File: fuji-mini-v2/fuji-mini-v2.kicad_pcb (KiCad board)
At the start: 2 copper layers, 58.4 x 81.3 mm, 59 parts, among them J1 Micro_SD_Card, J2 AudioJack3_SwitchT, J4 USB_C_Receptacle_USB2.0_14P, SW1 RotaryEncoder_Switch, U1 ESP32-S3, U2 PCM5102A, U3 TPA6110A2DGN, U4 ER_OLEDM0.91_1x-I2C, U5 MCP73831-2-MC, U6 AMS1117-3.3

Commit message: v2.0 2.0 Whole Remake
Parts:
- removed BCKWRD/FRWD1, PLAY/PAUSE1: SW_Push, Button_Switch_THT:SW_PUSH_6mm
- removed C23: 10uF, Capacitor_SMD:C_0805_2012Metric
- removed J4: USB_C_Receptacle_USB2.0_14P, Connector_USB:USB_C_Receptacle_XKB_U262-16XN-4BVC11
- removed SW1: RotaryEncoder_Switch, Rotary_Encoder:RotaryEncoder_Alps_EC11E-Switch_Vertical_H20mm
- added BOOT: SW_Push, Button_Switch_THT:SW_PUSH_6mm, F.Cu at (91.4, 134.9)
- added J3: USB_C, Connector_USB:USB_C_Receptacle_XKB_U262-16XN-4BVC11, F.Cu at (81.3, 146.1)
- added NEXT: SW_Push, Button_Switch_THT:SW_PUSH_6mm, F.Cu at (79.9, 106.0)
- added PLAY: SW_Push, Button_Switch_THT:SW_PUSH_6mm, F.Cu at (79.9, 94.6)
- added R22: 5.1k, Resistor_SMD:R_0805_2012Metric, F.Cu at (84.5, 137.8)
- added R23: 5.1k, Resistor_SMD:R_0805_2012Metric, F.Cu at (78.4, 137.8)
- added RESET: SW_Push, Button_Switch_THT:SW_PUSH_6mm, F.Cu at (91.4, 124.1)
- added VOLUME: RotaryEncoder_Switch, Rotary_Encoder:RotaryEncoder_Alps_EC11E-Switch_Vertical_H20mm, F.Cu at (144.1, 56.9)
- BT1: moved to B.Cu
- C1, C5: value 100nF -> 10uF
- C11, C16: value 100nF -> 2.2uF
- C14, C7, J1, R1, R12, R15, R17, R2, R3, R4, R8, R9: moved to F.Cu
- C15: value 1uF -> 100nF
- C17: value 100nF -> 220uF; footprint Capacitor_SMD:C_0805_2012Metric -> Capacitor_THT:CP_Radial_D6.3mm_P2.50mm
- C19: value 220uF -> 4.7uF; footprint Capacitor_THT:CP_Radial_D6.3mm_P2.50mm -> Capacitor_SMD:C_0805_2012Metric
- C20: value 1uF -> 10uF
- C21, C22: value 10uF -> 1uF
- C3: value 100nF -> 1uF
- R10: value 4.7k -> 20k; moved to F.Cu
- R11: value 4.7k -> 10k; moved to F.Cu
- R13, R14: value 10k -> 4.7k; moved to F.Cu
- R16: value 2k -> 10k; moved to F.Cu
- R18: value 5.1k -> 2k; moved to F.Cu
- R19: value 5.1k -> 10k; moved to F.Cu
- R20: value 10k -> 1k; moved to F.Cu
- R21: value 1k -> 10k; moved to F.Cu
- R5, R6, R7: value 20k -> 10k; moved to F.Cu
- U1: value ESP32-S3 -> ESP32-S3-WROOM-1; footprint Package_DFN_QFN:QFN-56-1EP_7x7mm_P0.4mm_EP4x4mm -> RF_Module:ESP32-S3-WROOM-1
- U6: value AMS1117-3.3 -> AP2112K-3.3; footprint Package_TO_SOT_SMD:SOT-223-3_TabPin2 -> Package_TO_SOT_SMD:SOT-23-5
- moved R13 74.7 mm to (99.3, 61.0), turned to 0 degrees
- moved BT1 72.5 mm to (78.2, 69.5), turned to -90 degrees
- moved R15 71.3 mm to (140.3, 80.0), turned to 0 degrees
- moved R19 57.0 mm to (145.8, 80.0), turned to 0 degrees
- moved J2 54.1 mm to (142.2, 135.3), turned to 0 degrees
- moved R18 53.5 mm to (78.5, 78.7), turned to 0 degrees
- moved D1 53.3 mm to (79.4, 61.6)
- moved R14 51.4 mm to (94.3, 61.0), turned to 0 degrees
- moved U5 50.4 mm to (80.9, 87.5)
- moved C2 49.2 mm to (140.3, 92.1)
- moved C4 48.6 mm to (87.0, 119.4)
- moved C17 47.3 mm to (132.1, 137.2)
- moved R10 46.1 mm to (137.2, 125.5), turned to 90 degrees
- moved C8 45.3 mm to (143.2, 123.2)
- moved C19 43.6 mm to (90.8, 87.3), turned to 90 degrees
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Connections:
- BT1 pad 2: 3V3 -> GND
- C1 pad 1: 3V3 -> +3V3
- C1 pad 2: Net-(J1-VDD) -> GND
- C10 pad 1: 3V3 -> GND
- C10 pad 2: 3V3 -> +3V3
- C11 pad 1: 3V3 -> Net-(U2-CAPP)
- C11 pad 2: 3V3 -> Net-(U2-CAPM)
- C12 pad 1: Net-(U2-CAPP) -> Net-(U3-BYPASS)
- C12 pad 2: Net-(U2-CAPM) -> GND
- C13 pad 1: Net-(U3-BYPASS) -> Net-(U2-OUTL)
- C13 pad 2: 3V3 -> DAC_OUTL
- C14 pad 1: Net-(U2-OUTL) -> Net-(U2-OUTR)
- C14 pad 2: DAC_OUTL -> DAC_OUTR
- C15 pad 1: Net-(U2-OUTR) -> Net-(U2-LDOO)
- C15 pad 2: DAC_OUTR -> GND
- C16 pad 1: Net-(U2-LDOO) -> Net-(U2-VNEG)
- C16 pad 2: 3V3 -> GND
- C17 pad 1: Net-(U2-VNEG) -> VO1
- C17 pad 2: 3V3 -> HP_L
- C18 pad 1: VO1 -> VO2
- C18 pad 2: HP_L -> HP_R
- C19 pad 1: VO2 -> GND
- C19 pad 2: HP_R -> VDD
- C2 pad 1: 3V3 -> +3V3
- C2 pad 2: 3V3 -> GND
- C20 pad 1: 3V3 -> GND
- C20 pad 2: VDD -> VBAT
- C21 pad 1: 3V3 -> GND
- C22 pad 1: 3V3 -> +3V3
- C22 pad 2: 3V3 -> GND
- C3 pad 1: 3V3 -> GND
- C3 pad 2: 3V3 -> Net-(U1-EN)
- C4 pad 1: 3V3 -> +3V3
- C4 pad 2: 3V3 -> GND
- C5 pad 1: 3V3 -> +3V3
- C5 pad 2: 3V3 -> GND
- C6 pad 1: 3V3 -> +3V3
- C6 pad 2: 3V3 -> GND
- C7 pad 1: 3V3 -> +3V3
- C7 pad 2: 3V3 -> GND
- C8 pad 1: 3V3 -> +3V3
- C8 pad 2: 3V3 -> GND
- C9 pad 1: 3V3 -> +3V3
- C9 pad 2: 3V3 -> GND
- D1 pad 2: 3V3 -> +3V3
- J1 pad 4: Net-(J1-VDD) -> +3V3
- J1 pad 6: 3V3 -> GND
- J1 pad SH: 3V3 -> GND
- J2 pad S: 3V3 -> GND
- J2 pad TN: HP_DETECT -> unconnected-(J2-PadTN)
- R1 pad 1: 3V3 -> GPIO11
- R1 pad 2: Net-(J1-DAT2) -> +3V3
- R10 pad 1: I2C_SCL -> DAC_OUTL
- R10 pad 2: 3V3 -> Net-(U3-IN1-)
- R11 pad 1: 3V3 -> VO1
- R11 pad 2: I2C_SDA -> Net-(U3-IN1-)
- R12 pad 1: 3V3 -> GND
- R12 pad 2: ENC_A -> AMP_ENABLE
- R13 pad 1: 3V3 -> I2C_SCL
- R13 pad 2: ENC_B -> +3V3
- R14 pad 1: BTN_PLAY -> +3V3
- R14 pad 2: 3V3 -> I2C_SDA
- R15 pad 1: 3V3 -> +3V3
- R15 pad 2: HP_DETECT -> ENC_A
- R16 pad 1: 3V3 -> +3V3
- R16 pad 2: Net-(U5-PROG) -> ENC_B
- R17 pad 1: Net-(R17-Pad1) -> BTN_PLAY
- R17 pad 2: 3V3 -> +3V3
- R18 pad 1: 3V3 -> GND
- R18 pad 2: Net-(J4-CC1) -> Net-(U5-PROG)
- R19 pad 1: 3V3 -> ENC_BTN
- R19 pad 2: Net-(J4-CC2) -> +3V3
- R2 pad 1: 3V3 -> +3V3
- R2 pad 2: Net-(J1-DAT1) -> GPIO10
- R20 pad 1: 3V3 -> Net-(U5-STAT)
- R20 pad 2: BTN_NEXT -> Net-(D1-K)
- R21 pad 1: Net-(U5-STAT) -> +3V3
- R21 pad 2: Net-(D1-K) -> BTN_NEXT
- R3 pad 1: Net-(U1-CHIP_PU) -> GPIO13
- R3 pad 2: 3V3 -> +3V3
- R4 pad 1: DAC_MUTE -> +3V3
- R4 pad 2: 3V3 -> Net-(U1-EN)
- R5 pad 1: DAC_OUTR -> +3V3
- R5 pad 2: Net-(U3-IN2-) -> Net-(J1-DAT1)
- R6 pad 1: VO2 -> +3V3
- R6 pad 2: Net-(U3-IN2-) -> Net-(J1-DAT2)
- R7 pad 1: DAC_OUTL -> DAC_MUTE
- R7 pad 2: Net-(U3-IN1-) -> GND
- R8 pad 1: VO1 -> DAC_OUTR
- R8 pad 2: Net-(U3-IN1-) -> Net-(U3-IN2-)
- R9 pad 1: 3V3 -> VO2
- R9 pad 2: AMP_ENABLE -> Net-(U3-IN2-)
- U1 pad 1: unconnected-(U1-LNA_IN-Pad1) -> GND
- U1 pad 10: I2S_BCK -> AMP_ENABLE
- U1 pad 11: I2S_DIN -> BTN_PLAY
- U1 pad 12: I2S_SCK -> I2C_SCL
- U1 pad 13: I2C_SCL -> USB_DN
- U1 pad 14: I2C_SDA -> USB_DP
- U1 pad 15: GPIO10 -> unconnected-(U1-IO3-Pad15)
- U1 pad 16: GPIO11 -> unconnected-(U1-IO46-Pad16)
- U1 pad 17: GPIO12 -> I2C_SDA
- U1 pad 18: GPIO13 -> GPIO10
- U1 pad 19: DAC_MUTE -> GPIO11
- U1 pad 2: 3V3 -> +3V3
- U1 pad 20: 3V3 -> GPIO12
- U1 pad 21: unconnected-(U1-XTAL_32K_P-Pad21) -> GPIO13
- U1 pad 22: unconnected-(U1-XTAL_32K_N-Pad22) -> DAC_MUTE
- U1 pad 23: AMP_ENABLE -> unconnected-(U1-IO21-Pad23)
- U1 pad 25: USB_DN -> unconnected-(U1-IO48-Pad25)
- U1 pad 26: USB_DP -> unconnected-(U1-IO45-Pad26)
- U1 pad 27: unconnected-(U1-GPIO21-Pad27) -> Net-(U1-IO0)
- U1 pad 29: 3V3 -> unconnected-(U1-IO36-Pad29)
- U1 pad 3: 3V3 -> Net-(U1-EN)
- U1 pad 38: unconnected-(U1-GPIO33-Pad38) -> ENC_B
- U1 pad 39: unconnected-(U1-GPIO34-Pad39) -> ENC_A
- U1 pad 4: Net-(U1-CHIP_PU) -> I2S_LRCK
- U1 pad 40: unconnected-(U1-GPIO35-Pad40) -> GND
- U1 pad 41: unconnected-(U1-GPIO36-Pad41) -> GND
- U1 pad 5: unconnected-(U1-GPIO0-Pad5) -> I2S_BCK
- U1 pad 6: unconnected-(U1-GPIO1-Pad6) -> I2S_DIN
- U1 pad 7: unconnected-(U1-GPIO2-Pad7) -> I2S_SCK
- U1 pad 8: unconnected-(U1-GPIO3-Pad8) -> ENC_BTN
- U1 pad 9: I2S_LRCK -> BTN_NEXT
- U2 pad 1: 3V3 -> +3V3
- U2 pad 10: 3V3 -> GND
- U2 pad 11: 3V3 -> GND
- U2 pad 16: 3V3 -> GND
- U2 pad 19: 3V3 -> GND
- U2 pad 20: 3V3 -> +3V3
- U2 pad 3: 3V3 -> GND
- U2 pad 8: 3V3 -> +3V3
- U2 pad 9: 3V3 -> GND
- U3 pad 2: 3V3 -> GND
- U3 pad 6: 3V3 -> +3V3
- U3 pad 9: 3V3 -> GND
- U4 pad 1: 3V3 -> GND
- U4 pad 2: 3V3 -> +3V3
- U5 pad 6: 3V3 -> GND
- U6 pad 1: 3V3 -> VBAT
- U6 pad 2: 3V3 -> GND
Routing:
- net 3V3: track 685.5 -> 0.00 mm, vias 16 -> 0
- net GND: track 0.00 -> 596.1 mm, vias 0 -> 14
- net +3V3: track 0.00 -> 353.4 mm, vias 0 -> 17
- net Net-(U2-VNEG): track 151.2 -> 12.8 mm, vias 2 -> 0
- net BTN_NEXT: track 10.6 -> 144.3 mm, vias 0 -> 2
- net ENC_B: track 4.21 -> 113.6 mm, vias 0 -> 2
- net ENC_A: track 4.35 -> 112.6 mm, vias 0 -> 2
- net Net-(D1-K): track 119.7 -> 17.7 mm, vias 0 -> 2
- net Net-(U2-CAPM): track 103.9 -> 9.84 mm, vias 2 -> 0
- net I2C_SCL: track 38.8 -> 129.9 mm, vias 1 -> 2
- net ENC_BTN: track 0.00 -> 88.7 mm, vias 0 -> 2
- net BTN_PLAY: track 11.4 -> 94.8 mm, vias 0 -> 3
- net I2C_SDA: track 49.4 -> 132.7 mm, vias 1 -> 2
- net Net-(U1-IO0): track 0.00 -> 73.0 mm
- net I2S_LRCK: track 115.4 -> 45.9 mm, vias 6 -> 4
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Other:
- board size 58.4 x 81.3 mm -> 73.8 x 97.7 mm
- board text removed: "Made by A41K"

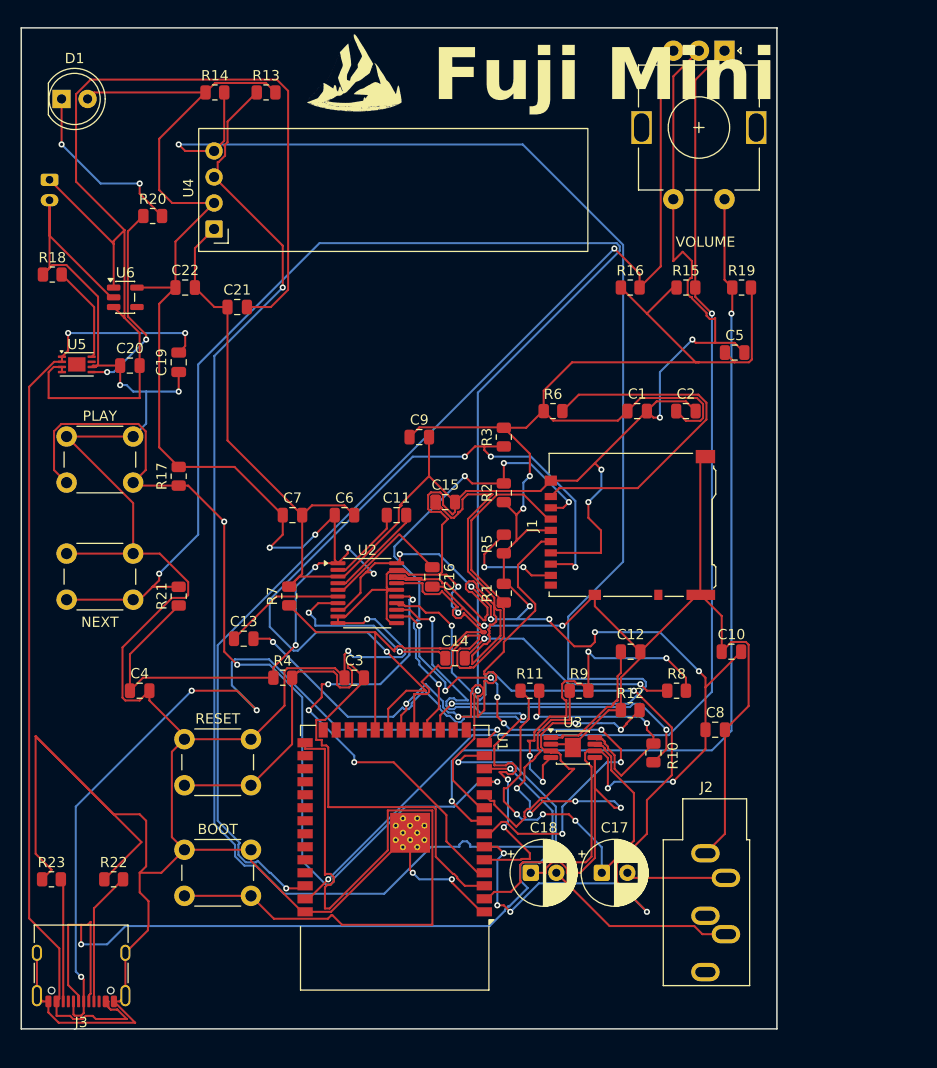
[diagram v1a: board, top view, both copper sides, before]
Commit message: Added 3D models / Fixed PCB positions
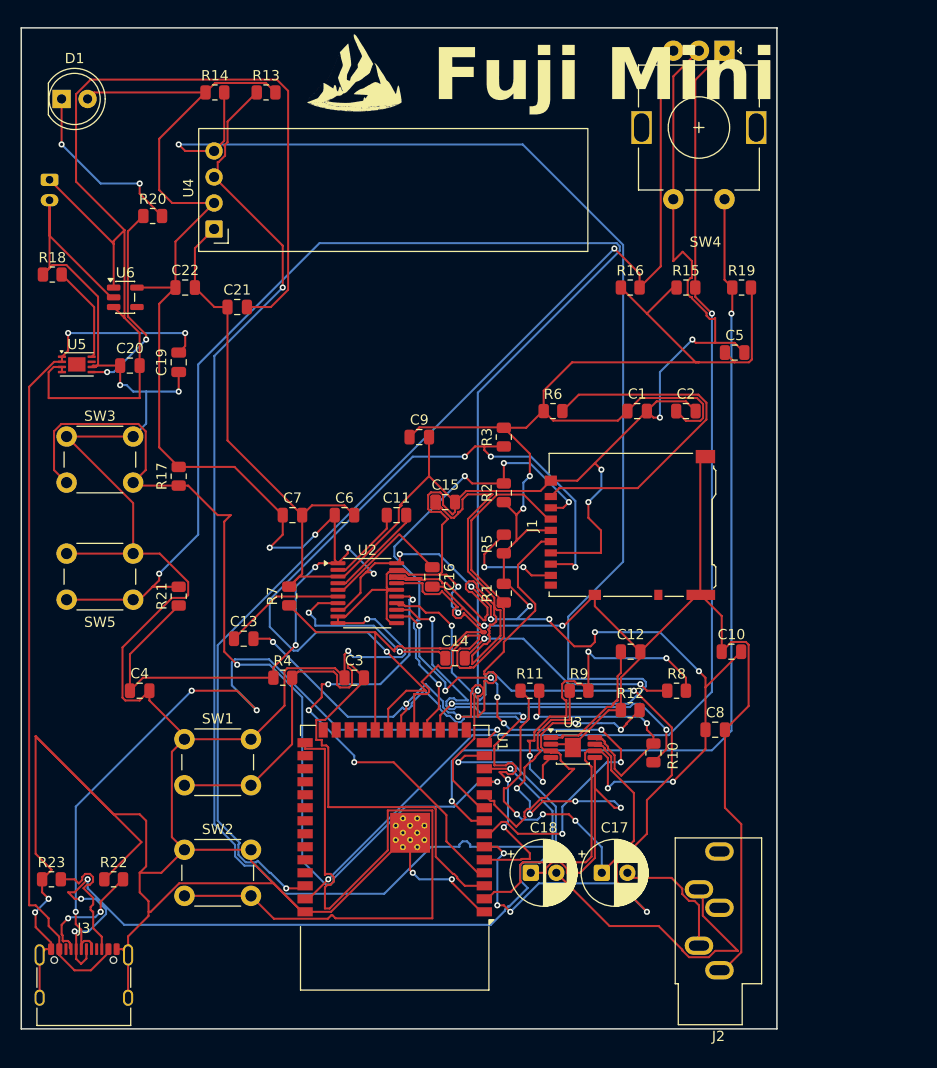
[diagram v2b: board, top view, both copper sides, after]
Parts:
- J3: value USB_C -> USB_C_Receptacle_USB2.0_14P
- moved J2 11.5 mm to (143.6, 146.7), turned to 180 degrees
- moved J3 2.25 mm to (81.5, 148.3), turned to 0 degrees
- renumbered RESET to SW1, BOOT to SW2, PLAY to SW3, VOLUME to SW4, NEXT to SW5
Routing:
- net GND: track 596.1 -> 621.3 mm, vias 14 -> 16
- net HP_R: track 19.0 -> 29.0 mm
- net VDD: track 94.0 -> 84.4 mm
- net USB_DP: track 82.4 -> 76.0 mm
- net USB_DN: track 90.8 -> 87.9 mm, vias 2 -> 4
- net HP_L: track 9.83 -> 12.6 mm
- net Net-(J3-CC1): track 13.1 -> 11.5 mm, vias 0 -> 2
- net BTN_PLAY: track 94.8 -> 96.1 mm, vias 3 -> 2
- net Net-(U1-IO0): track 73.0 -> 72.1 mm
- net Net-(J3-CC2): track 12.0 -> 12.9 mm

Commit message: Finished / Started the README / Added new gerbers
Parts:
- Headphone Jack: renamed from J2
- renumbered J3 to USB-C
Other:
- board text added: "v1.0"
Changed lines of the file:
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@@
 		(tags "tact sw push 6mm")
 		(property "Reference" "SW5"
-			(at 3.25 6.695 0)
+			(at 3.25 -2.485 0)
 			(layer "F.SilkS")
 			(effects
@@
 		(descr "USB Type C, right-angle, SMT, https://datasheet.lcsc.com/szlcsc/1811141824_XKB-Enterprise-U262-161N-4BVC11_C319148.pdf")
 		(tags "USB C Type-C Receptacle SMD")
-		(property "Reference" "J3"
+		(property "Reference" "USB-C"
 			(at 0 -5.715 0)
 			(layer "F.SilkS")
@@
 		(descr "TRS 3.5mm, horizontal, through-hole, with switch, https://www.cui.com/product/resource/sj1-353xng.pdf")
 		(tags "TRS audio jack stereo horizontal")
-		(property "Reference" "J2"
-			(at 0.1 -6.45 0)
+		(property "Reference" "Headphone Jack"
+			(at 5.815 0.625 90)
 			(layer "F.SilkS")
 			(effects
@@
 				)
 			)
+		)
+	)
+	(gr_text "v1.0"
+		(at 147.955 95.885 90)
+		(layer "F.SilkS")
+		(effects
+			(font
+				(face "Gadugi")
+				(size 2 2)
+				(thickness 0.3048)
+				(bold yes)
+			)
+			(justify left bottom)
+		)
+		(render_cache "v1.0" 90
+			(polygon
+				(pts
+					(xy 146.215976 94.371182) (xy 147.615 94.891664) (xy 147.615 95.383569) (xy 146.215976 95.879504)
+					(xy 146.215976 95.417763) (xy 147.078032 95.174619) (xy 147.219638 95.140928) (xy 147.326671 95.126748)
+					(xy 147.326671 95.121252) (xy 147.224676 95.105221) (xy 147.086214 95.070694) (xy 146.215976 94.822055)
+				)
+			)
+			(polygon
+				(pts
+					(xy 145.614162 93.232034) (xy 147.615 93.232034) (xy 147.615 93.66239) (xy 146.100083 93.66239)
+					(xy 146.159434 93.746409) (xy 146.209993 93.849602) (xy 146.248217 93.96293) (xy 146.270687 94.079068)
+					(xy 145.911161 94.079068) (xy 145.854223 93.914988) (xy 145.784155 93.762163) (xy 145.70186 93.618665)
+					(xy 145.614162 93.493007)
+				)
+			)
+			(polygon
+				(pts
+					(xy 147.646263 92.384389) (xy 147.638621 92.452784) (xy 147.616636 92.511232) (xy 147.580317 92.561953)
+					(xy 147.532604 92.601687) (xy 147.47926 92.625055) (xy 147.418262 92.633028) (xy 147.355644 92.624731)
+					(xy 147.302408 92.600658) (xy 147.256207 92.56) (xy 147.221516 92.508127) (xy 147.20034 92.448052)
+					(xy 147.192948 92.37755) (xy 147.200496 92.306171) (xy 147.221938 92.24665) (xy 147.256817 92.196444)
+					(xy 147.303238 92.157306) (xy 147.356317 92.134093) (xy 147.418262 92.126102) (xy 147.481884 92.134306)
+					(xy 147.535803 92.158038) (xy 147.582393 92.197909) (xy 147.617144 92.249023) (xy 147.638652 92.310273)
+				)
+			)
+			(polygon
+				(pts
+					(xy 146.826795 90.49439) (xy 147.002499 90.51954) (xy 147.151111 90.558536) (xy 147.276367 90.609664)
+					(xy 147.381503 90.67188) (xy 147.477102 90.753245) (xy 147.550055 90.845563) (xy 147.602489 90.950208)
+					(xy 147.634932 91.069549) (xy 147.646263 91.206772) (xy 147.634375 91.352265) (xy 147.600724 91.475667)
+					(xy 147.546941 91.581031) (xy 147.47273 91.671359) (xy 147.375905 91.748349) (xy 147.252577 91.812238)
+					(xy 147.097427 91.861787) (xy 146.903973 91.894398) (xy 146.664773 91.906284) (xy 146.452276 91.897109)
+					(xy 146.272635 91.871489) (xy 146.121412 91.83186) (xy 145.994621 91.780033) (xy 145.888813 91.717117)
+					(xy 145.792846 91.634701) (xy 145.719369 91.540616) (xy 145.666379 91.433377) (xy 145.633491 91.31047)
+					(xy 145.623523 91.187599) (xy 145.95024 91.187599) (xy 145.963705 91.259708) (xy 146.004286 91.321303)
+					(xy 146.0783 91.375567) (xy 146.19876 91.421563) (xy 146.383602 91.454719) (xy 146.654637 91.467745)
+					(xy 146.908315 91.455152) (xy 147.081944 91.423035) (xy 147.195693 91.37832) (xy 147.266093 91.325259)
+					(xy 147.305011 91.264582) (xy 147.318 91.193094) (xy 147.305049 91.124457) (xy 147.265924 91.065682)
+					(xy 147.194339 91.013756) (xy 147.077509 90.969643) (xy 146.897877 90.937802) (xy 146.63412 90.925282)
+					(xy 146.369544 90.937632) (xy 146.189681 90.96901) (xy 146.073012 91.012403) (xy 146.001791 91.063333)
+					(xy 145.96303 91.120758) (xy 145.95024 91.187599) (xy 145.623523 91.187599) (xy 145.621978 91.168548)
+					(xy 145.633798 91.027936) (xy 145.667334 90.908308) (xy 145.721127 90.805746) (xy 145.795698 90.717399)
+					(xy 145.893489 90.641732) (xy 146.018654 90.578671) (xy 146.176776 90.529597) (xy 146.374598 90.497219)
+					(xy 146.619832 90.485401)
+				)
+			)

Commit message: Finishing up the designs / Fixing Issues / Trying new things
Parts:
- added G***: LOGO, LOGO, F.Cu at (83.2, 92.1)
- added G***: LOGO, LOGO, F.Cu at (83.2, 103.5)
- C22: value 1uF -> 10uF
- J2: renamed from Headphone Jack
- moved G*** 26.1 mm to (109.9, 84.2)
- renumbered USB-C to J3
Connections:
- D1 pad 2: +3V3 -> VBAT
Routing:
- net VBAT: track 108.0 -> 215.5 mm
- net I2C_SCL: track 129.9 -> 204.8 mm
- net I2C_SDA: track 132.7 -> 159.6 mm
- net ENC_B: track 113.6 -> 133.3 mm
- net GND: track 621.3 -> 603.1 mm
- net +3V3: track 353.4 -> 341.6 mm
- net BTN_NEXT: track 144.3 -> 155.7 mm
- net Net-(U1-IO0): track 72.1 -> 61.8 mm
- net ENC_A: track 112.6 -> 120.5 mm
- net I2S_DIN: track 84.1 -> 89.3 mm
- net GPIO13: track 77.8 -> 81.5 mm
- net USB_DP: track 76.0 -> 79.5 mm
- net Net-(J1-DAT2): track 35.0 -> 38.1 mm
- net I2S_BCK: track 49.1 -> 46.2 mm
- net Net-(U1-EN): track 67.7 -> 65.5 mm
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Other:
- board text added: "@A41K"
- board text added: "BOOT"
- board text added: "CHARGE"
- board text added: "RESET"
- board text added: "SCREEN"
- board text added: "VOLUME/SELECT"
